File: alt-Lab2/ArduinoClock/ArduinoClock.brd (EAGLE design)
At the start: 54.2 x 17.8 mm, 40 parts, among them IC1 DS3231/SO, U1 MIC5225-5.0, U2 ATMEGA328P, U3 CP2104, U4 MIC5225-3.3, X1 20329, Y2 CSTCE16M0V53-R0 16MHZ

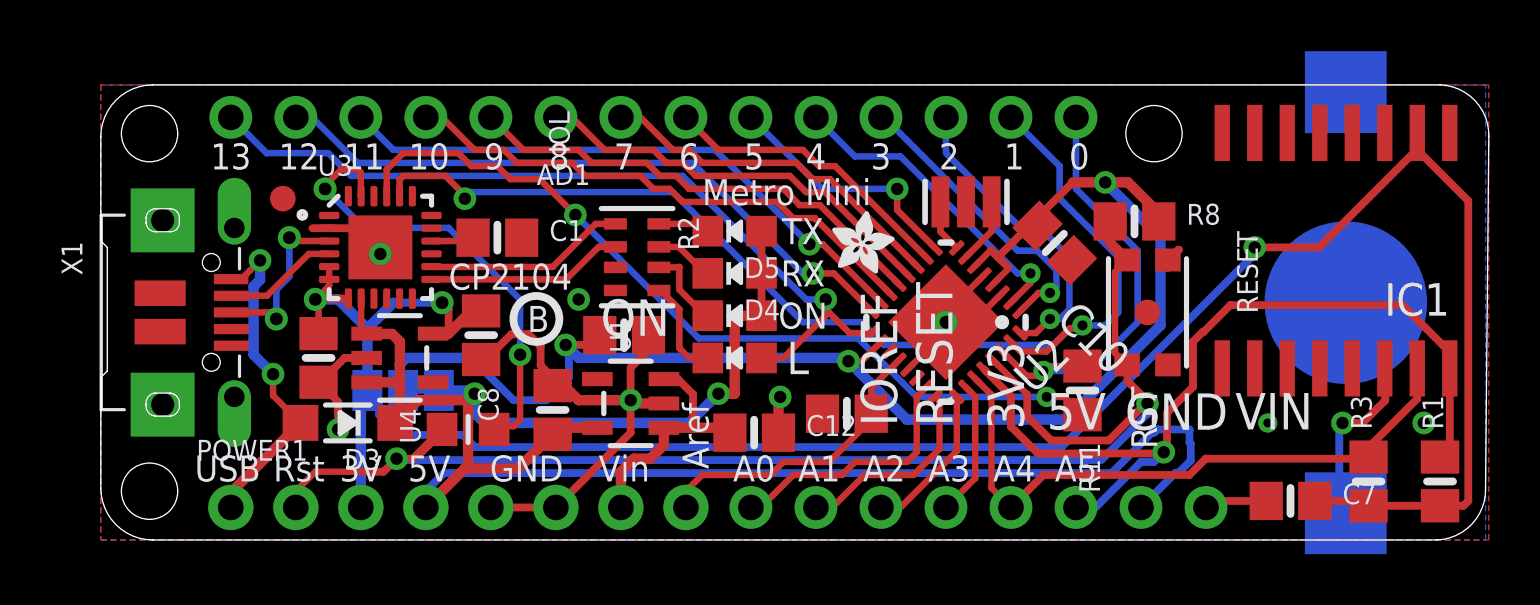
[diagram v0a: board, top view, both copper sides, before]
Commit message: fixed some ground planes and airwired
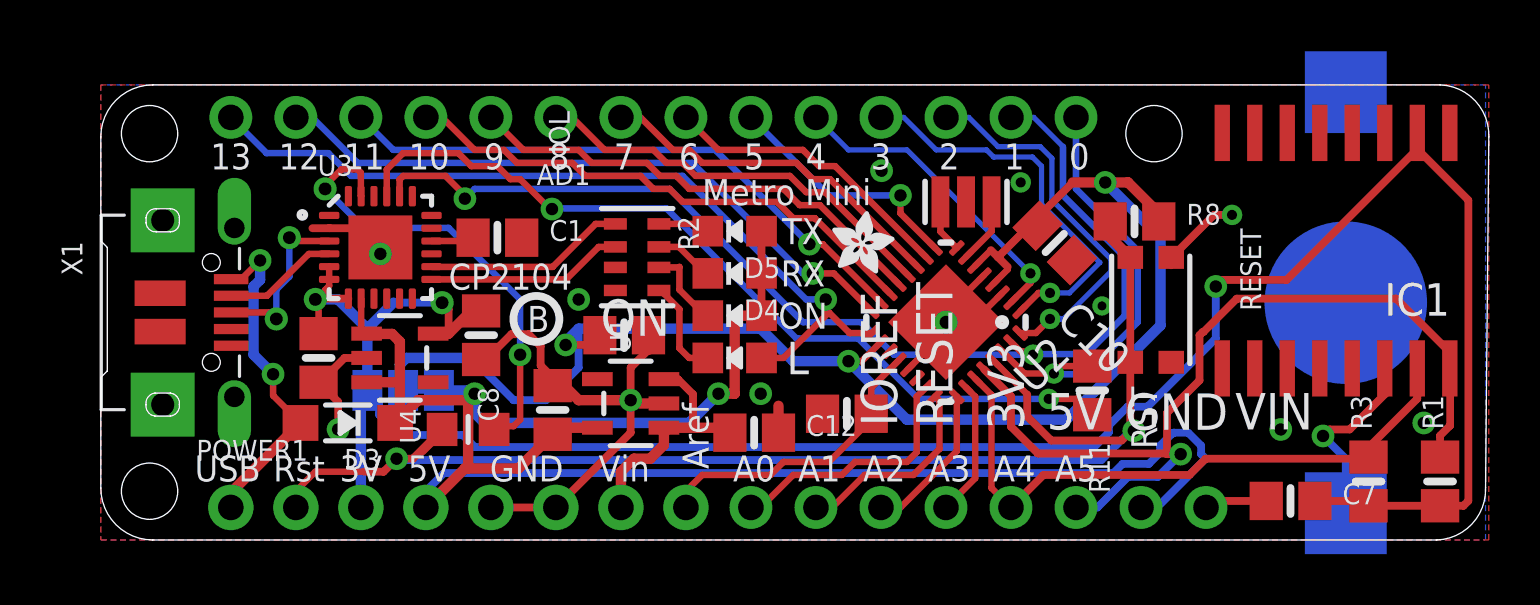
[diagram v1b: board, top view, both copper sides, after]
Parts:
- removed FD1, FD2: FIDUCIAL"", microbuilder:FIDUCIAL_1MM
- moved R11 0.38 mm to (38.7, 5.84)
- moved RESET 0.16 mm to (41.0, 8.99)
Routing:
- net IO3: track 11.8 -> 15.9 mm
- net AD5/SCL: track 33.3 -> 36.5 mm
- net IO2: track 12.3 -> 15.1 mm
- net GND: track 43.5 -> 46.0 mm, vias 8 -> 12
- net RESET: track 55.9 -> 54.0 mm
- net VCCIO: track 57.2 -> 58.5 mm
- net VBAT: track 6.27 -> 7.50 mm
- net 3.3V: track 89.9 -> 91.1 mm
- net TXD: track 45.1 -> 44.2 mm
- net +5V: track 77.9 -> 78.6 mm
